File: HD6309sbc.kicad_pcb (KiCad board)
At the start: 2 copper layers, 99.8 x 99.8 mm, 29 parts, among them J1 Conn_01x02_Male, J2 Conn_02x30_Odd_Even, J3 Conn_01x02_Male, U1 HD63C09, U10 74HC375, U11 74HC02, U12 74HC21, U13 74HC21, U2 74HC163, U3 74HC04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

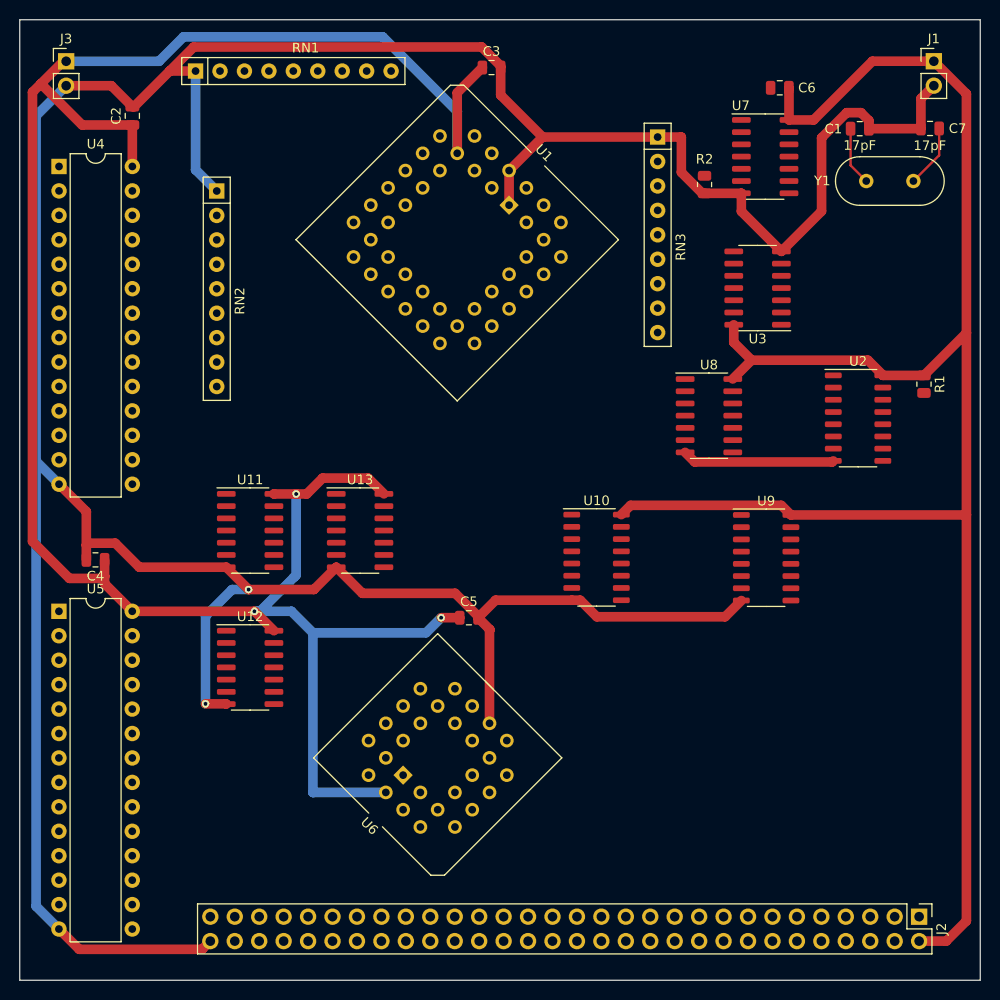
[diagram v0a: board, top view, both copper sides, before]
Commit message: add paged memory
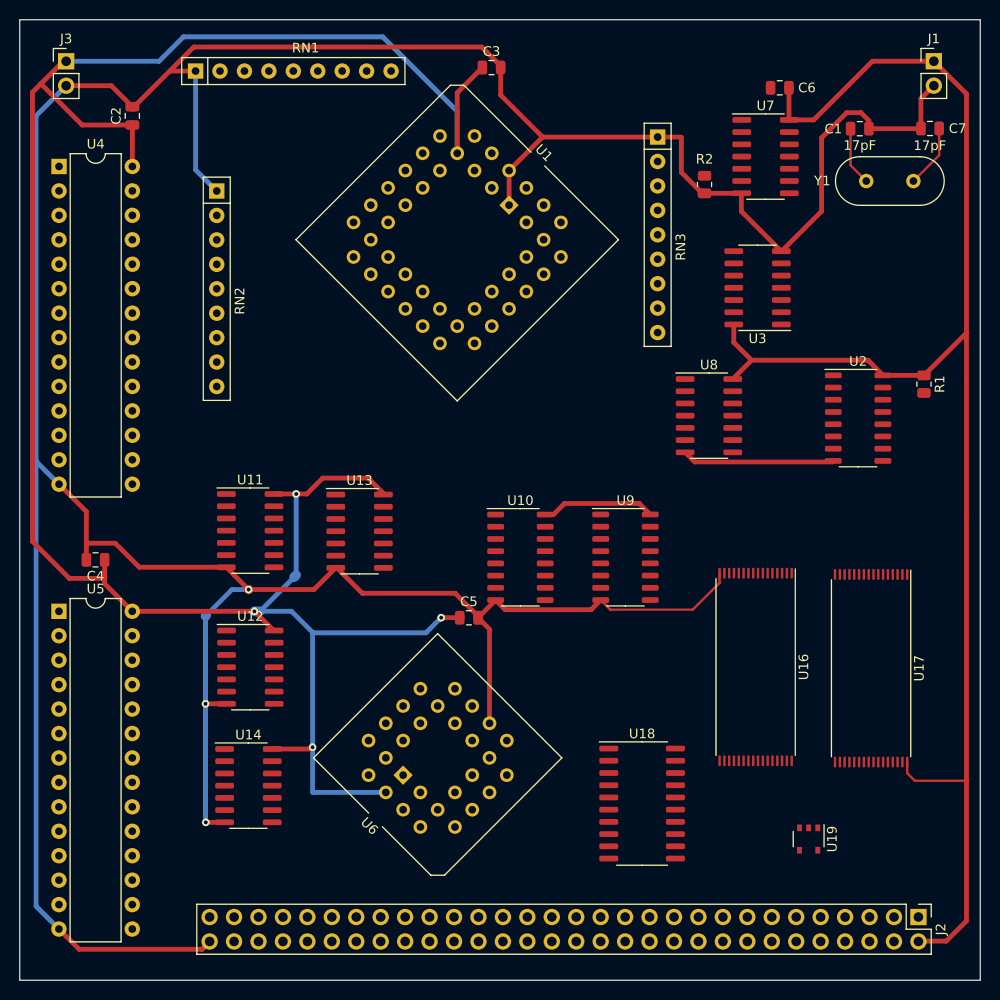
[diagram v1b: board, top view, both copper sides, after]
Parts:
- added U14: 74HC02, Package_SO:SO-14_3.9x8.65mm_P1.27mm, F.Cu at (49.2, 105.0)
- added U16: AS6C4008-55PCN, Package_SO:TSOP-I-32_18.4x8mm_P0.5mm, F.Cu at (101.9, 92.7)
- added U17: AS6C4008-55PCN, Package_SO:TSOP-I-32_18.4x8mm_P0.5mm, F.Cu at (113.9, 92.8)
- added U18: 74LS244, Package_SO:SO-20_5.3x12.6mm_P1.27mm, F.Cu at (90.1, 106.9)
- added U19: 74AHC1G86, Package_SO:TSOP-5_1.65x3.05mm_P0.95mm, F.Cu at (107.4, 110.5)
- U3: value 74HC04 -> 74HC02
- moved U9 14.6 mm to (88.3, 81.3)
- moved U10 7.91 mm to (77.4, 81.3)
- moved U13 0.09 mm to (60.7, 78.6)
- moved J2 0.08 mm to (118.8, 118.6)
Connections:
- U3 pad 1: Net-(C1-Pad1) -> E
- U3 pad 10: unconnected-(U3-Pad10) -> ~{E}
- U3 pad 11: unconnected-(U3-Pad11) -> Clock3
- U3 pad 12: unconnected-(U3-Pad12) -> Clock3
- U3 pad 13: unconnected-(U3-Pad13) -> ~{Q}
- U3 pad 2: Net-(U3-Pad2) -> Clock3
- U3 pad 3: Net-(U3-Pad2) -> Clock6
- U3 pad 5: Clock12 -> Net-(C1-Pad1)
- U3 pad 6: ~{Clock12} -> Net-(C1-Pad1)
- U3 pad 8: unconnected-(U3-Pad8) -> E
- U3 pad 9: unconnected-(U3-Pad9) -> E
- U7 pad 10: unconnected-(U7-Pad10) -> Net-(U7-Pad10)
- U7 pad 11: unconnected-(U7-Pad11) -> A15
- U7 pad 12: unconnected-(U7-Pad12) -> Net-(U7-Pad12)
- U7 pad 13: unconnected-(U7-Pad13) -> P5
- U8 pad 10: unconnected-(U8-Pad10) -> Net-(U7-Pad10)
- U8 pad 8: unconnected-(U8-Pad8) -> ~{BS}
- U8 pad 9: unconnected-(U8-Pad9) -> A14
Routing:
- net GND: track 386.4 -> 400.0 mm, vias 2 -> 3
- net +5V: track 418.0 -> 404.8 mm, vias 3 -> 4

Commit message: add power routing
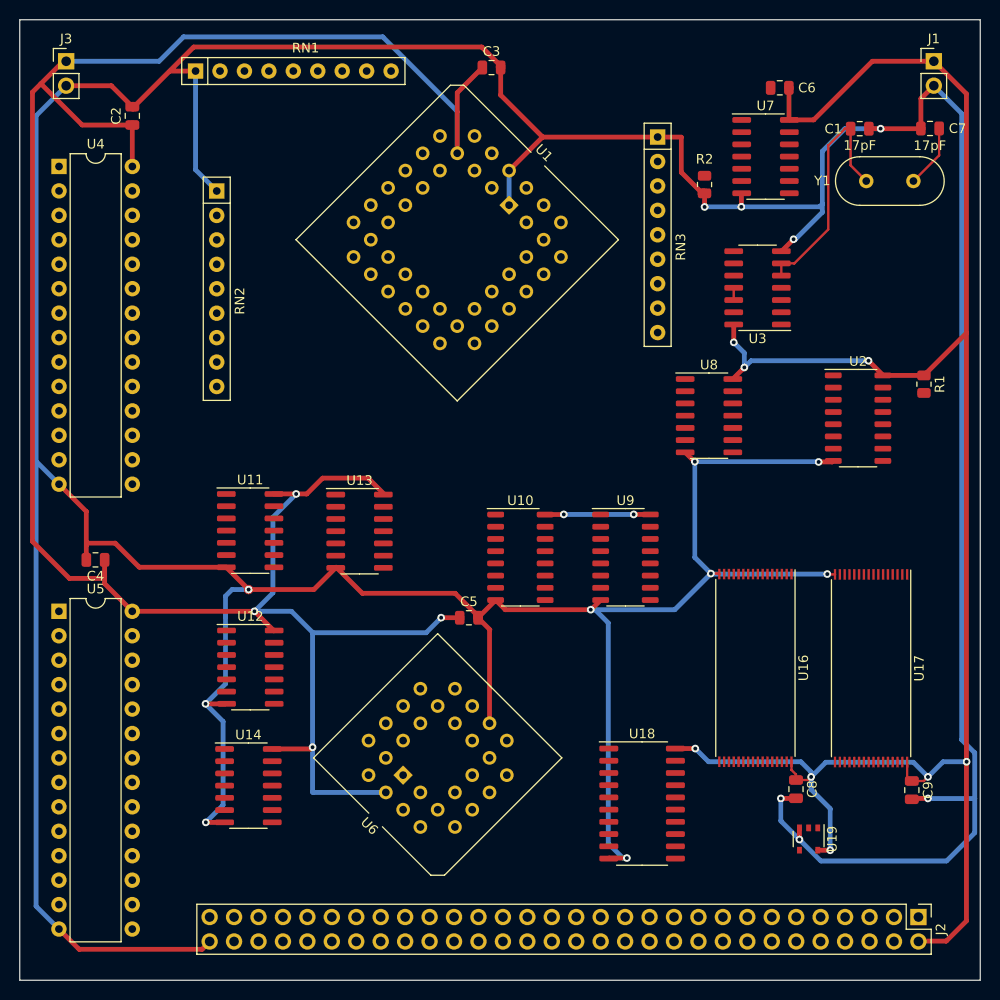
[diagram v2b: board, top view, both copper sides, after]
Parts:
- added C8: 1uF, Capacitor_SMD:C_0805_2012Metric, F.Cu at (106.1, 105.4)
- added C9: 1uF, Capacitor_SMD:C_0805_2012Metric, F.Cu at (118.1, 105.5)
- C3: value C -> 1uF
- moved U16 0.10 mm to (101.9, 92.8)
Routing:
- net GND: track 400.0 -> 572.9 mm, vias 3 -> 16
- net +5V: track 404.8 -> 447.9 mm, vias 4 -> 14
- net Net-(C1-Pad1): track 6.11 -> 25.5 mm
- net Clock3: track 0.00 -> 1.27 mm

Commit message: move rom for clearance
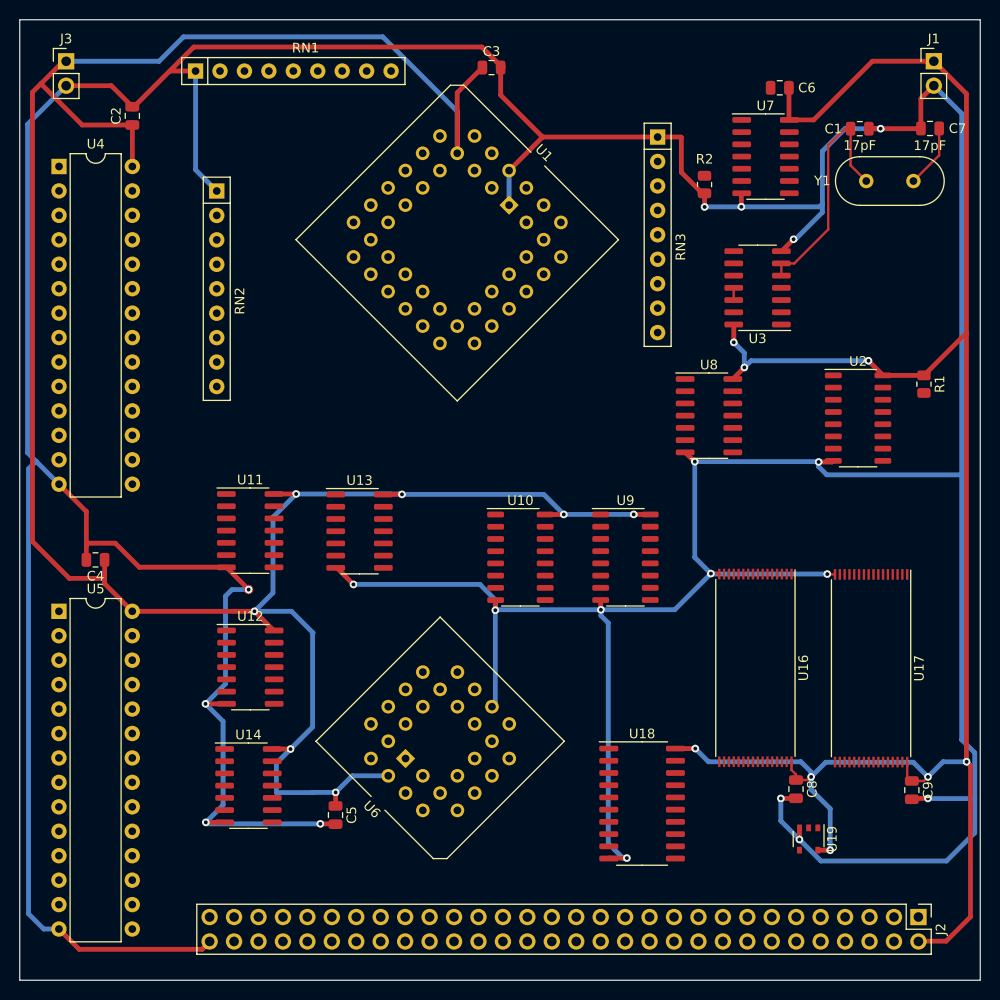
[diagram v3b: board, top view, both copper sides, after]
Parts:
- moved C5 24.7 mm to (58.2, 108.1), turned to -90 degrees
- moved U6 1.75 mm to (65.5, 102.2)
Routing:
- net GND: track 572.9 -> 592.2 mm, vias 16 -> 19
- net +5V: track 447.9 -> 457.8 mm, vias 14 -> 15

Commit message: rearrange components for routing
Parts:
- moved RN1 105.6 mm to (108.7, 113.9), turned to 180 degrees
- moved RN3 87.8 mm to (109.6, 123.5), turned to 180 degrees
- moved RN2 82.7 mm to (65.5, 123.5), turned to 0 degrees
- moved C5 77.9 mm to (47.5, 30.9), turned to 180 degrees
- moved U6 65.1 mm to (53.4, 38.2), turned to 45 degrees
- moved U1 46.9 mm to (73.3, 91.5)
- moved C3 45.9 mm to (69.8, 76.0)
- moved U18 23.6 mm to (86.2, 83.6), turned to -90 degrees
- moved U9 16.0 mm to (82.3, 66.4)
- moved U10 16.0 mm to (71.4, 66.5)
- moved U13 12.5 mm to (56.0, 67.0)
- moved U11 11.8 mm to (46.7, 67.0)
- moved U12 11.8 mm to (46.7, 81.2)
- moved U14 11.8 mm to (46.5, 93.5)
- moved C9 3.71 mm to (118.5, 101.8)
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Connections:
- J2 pad 35: Q3 -> unconnected-(J2-Pad35)
- J2 pad 37: Q4 -> unconnected-(J2-Pad37)
- J2 pad 39: Q5 -> unconnected-(J2-Pad39)
- J2 pad 41: Q6 -> unconnected-(J2-Pad41)
- J2 pad 43: Q7 -> unconnected-(J2-Pad43)
- RN2 pad 2: A13 -> A15
- RN2 pad 3: A8 -> A14
- RN2 pad 4: A9 -> A13
- RN2 pad 5: A11 -> A12
- RN2 pad 6: A10 -> A11
- RN2 pad 7: A15 -> A10
- RN2 pad 8: A1 -> A9
- RN2 pad 9: A0 -> A8
- RN3 pad 2: A2 -> A0
- RN3 pad 3: A3 -> A1
- RN3 pad 4: A12 -> A2
- RN3 pad 5: A14 -> A3
- U10 pad 11: Q6 -> P3
- U10 pad 13: Q7 -> P4
- U10 pad 3: Q4 -> P1
- U10 pad 5: Q5 -> P2
- U9 pad 13: Q3 -> P0
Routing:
- net +5V: track 457.8 -> 522.5 mm, vias 15 -> 18
- net GND: track 592.2 -> 643.8 mm, vias 19 -> 22

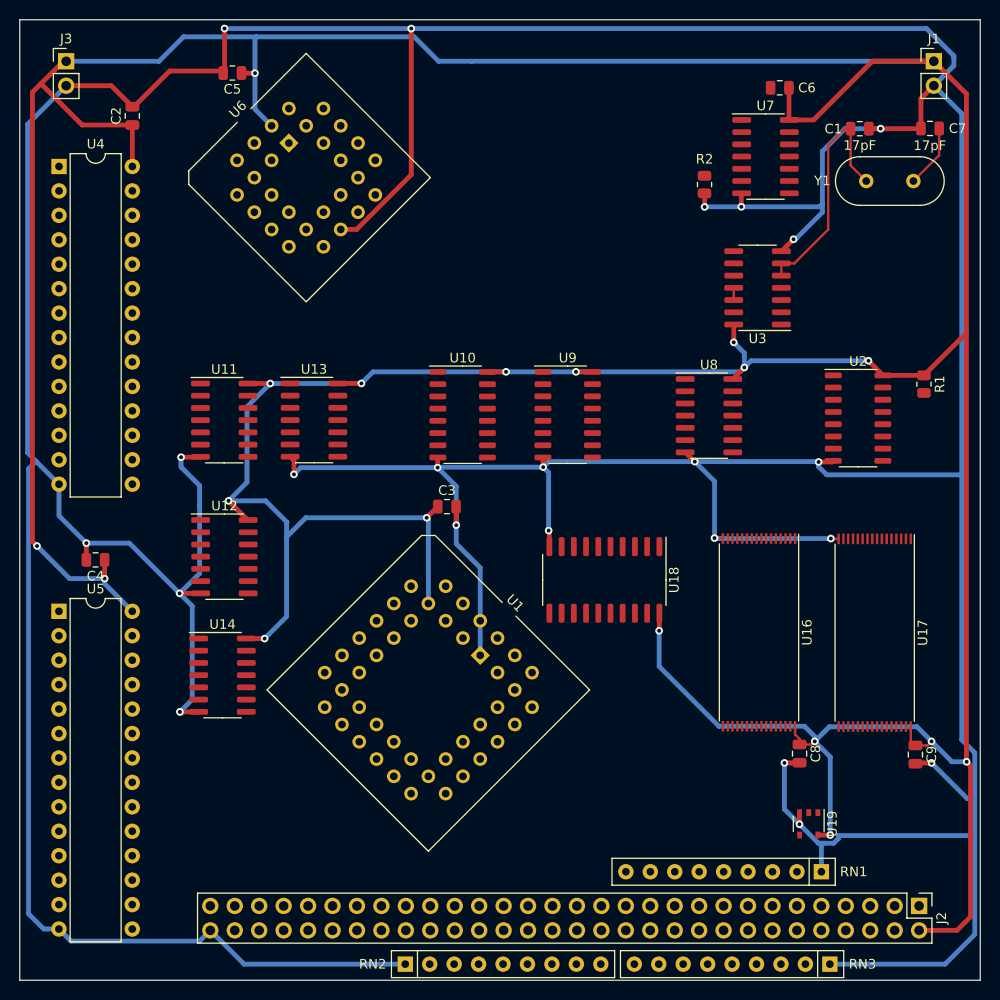
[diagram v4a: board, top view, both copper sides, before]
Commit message: reduce component count
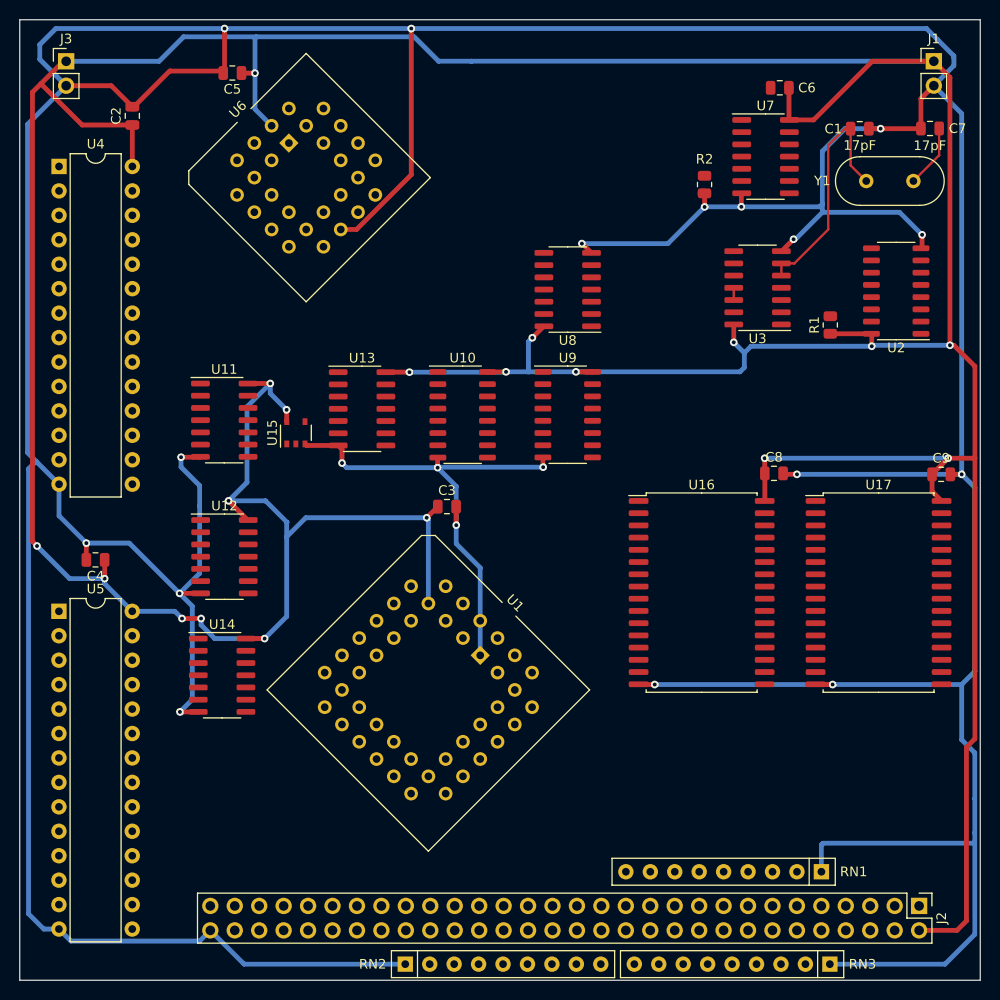
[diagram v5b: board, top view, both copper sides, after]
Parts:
- removed U18: 74LS244, Package_SO:SO-20_5.3x12.6mm_P1.27mm
- removed U19: 74AHC1G86, Package_SO:TSOP-5_1.65x3.05mm_P0.95mm
- added U15: 74AHC1G08, Package_SO:TSOP-5_1.65x3.05mm_P0.95mm, F.Cu at (54.1, 68.3)
- U16, U17: footprint Package_SO:TSOP-I-32_18.4x8mm_P0.5mm -> Package_SO:SSOP-32_11.305x20.495mm_P1.27mm
- moved C9 29.2 mm to (121.2, 72.6), turned to 0 degrees
- moved C8 29.2 mm to (103.8, 72.5), turned to 0 degrees
- moved U8 19.7 mm to (82.3, 53.4), turned to 180 degrees
- moved U2 13.8 mm to (116.5, 53.6), turned to 180 degrees
- moved R1 11.5 mm to (109.6, 57.1), turned to 90 degrees
- moved U16 7.25 mm to (96.3, 84.9), turned to 0 degrees
- moved U13 5.13 mm to (61.0, 65.8)
- moved U17 4.19 mm to (114.7, 84.9), turned to 0 degrees
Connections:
- U11 pad 11: A6 -> unconnected-(U11-Pad11)
- U11 pad 12: A7 -> unconnected-(U11-Pad12)
- U11 pad 13: Net-(U11-Pad13) -> unconnected-(U11-Pad13)
- U11 pad 5: A2 -> A3
- U11 pad 6: A3 -> A4
- U11 pad 8: A4 -> A6
- U11 pad 9: A5 -> A7
- U13 pad 5: Net-(U11-Pad13) -> Net-(U13-Pad5)
- U14 pad 1: ~{OEa} -> (no net)
- U14 pad 2: Net-(U14-Pad2) -> (no net)
- U14 pad 3: ~{OE} -> (no net)
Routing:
- net +5V: track 522.5 -> 502.2 mm, vias 18 -> 19
- net GND: track 643.8 -> 652.3 mm, vias 22 -> 20

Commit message: move paged memory to external board
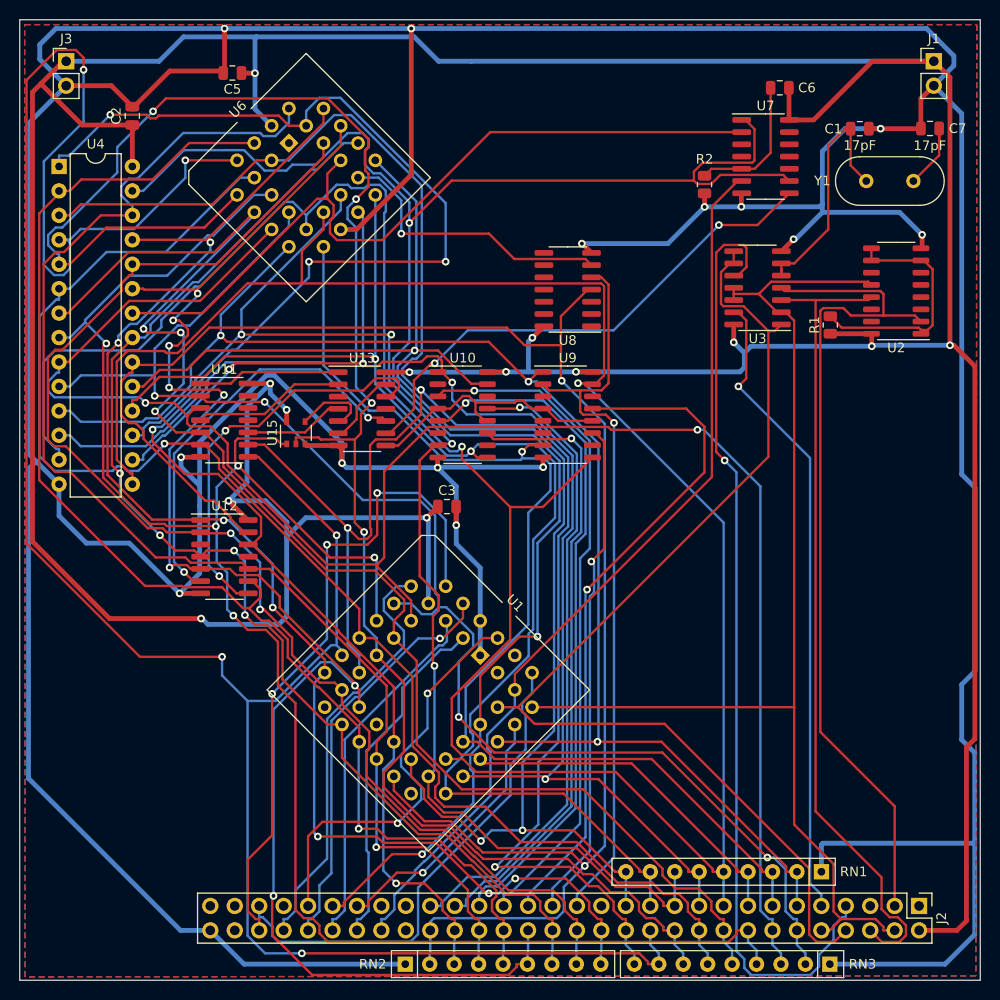
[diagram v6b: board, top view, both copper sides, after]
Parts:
- removed C4, C8, C9: 1uF, Capacitor_SMD:C_0805_2012Metric
- removed U14: 74HC02, Package_SO:SO-14_3.9x8.65mm_P1.27mm
- removed U16, U17: AS6C4008-55PCN, Package_SO:SSOP-32_11.305x20.495mm_P1.27mm
- removed U5: UM61256FK, Package_DIP:DIP-28_W7.62mm
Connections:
- J2 pad 35: unconnected-(J2-Pad35) -> Q3
- J2 pad 37: unconnected-(J2-Pad37) -> Q4
- J2 pad 39: unconnected-(J2-Pad39) -> Q5
- J2 pad 41: unconnected-(J2-Pad41) -> Q6
- J2 pad 43: unconnected-(J2-Pad43) -> Q7
- J2 pad 45: unconnected-(J2-Pad45) -> Q8
- U10 pad 11: P3 -> Q5
- U10 pad 13: P4 -> Q6
- U10 pad 3: P1 -> Q3
- U10 pad 5: P2 -> Q4
- U7 pad 10: Net-(U7-Pad10) -> (no net)
- U7 pad 11: A15 -> (no net)
- U7 pad 12: Net-(U14-Pad6) -> (no net)
- U7 pad 13: P5 -> (no net)
- U8 pad 1: A15 -> unconnected-(U8-Pad1)
- U8 pad 10: Net-(U7-Pad10) -> (no net)
- U8 pad 2: ~{ROM}/RAM -> unconnected-(U8-Pad2)
- U8 pad 3: Net-(U5-Pad20) -> unconnected-(U8-Pad3)
- U8 pad 8: ~{BS} -> (no net)
- U8 pad 9: A14 -> (no net)
- U9 pad 11: Q2 -> Q1
- U9 pad 13: P0 -> Q2
- U9 pad 2: ~{ROM}/RAM -> ROM/~{RAM}
- U9 pad 3: ROM/~{RAM} -> ~{ROM}/RAM
- U9 pad 5: Q1 -> Q0
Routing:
- net A6: track 0.00 -> 248.7 mm, vias 0 -> 5
- net A7: track 0.00 -> 204.9 mm, vias 0 -> 3
- net A2: track 0.00 -> 197.7 mm, vias 0 -> 5
- net R/~{W}: track 0.00 -> 192.6 mm, vias 0 -> 3
- net A5: track 0.00 -> 188.8 mm, vias 0 -> 4
- net A1: track 0.00 -> 188.3 mm, vias 0 -> 2
- net A15: track 0.00 -> 185.0 mm, vias 0 -> 2
- net D3: track 0.00 -> 183.8 mm, vias 0 -> 1
- net D2: track 0.00 -> 175.5 mm, vias 0 -> 1
- net A14: track 0.00 -> 170.2 mm, vias 0 -> 5
- net A11: track 0.00 -> 165.1 mm, vias 0 -> 8
- net D7: track 0.00 -> 159.5 mm, vias 0 -> 3
- net A3: track 0.00 -> 152.1 mm, vias 0 -> 3
- net D0: track 0.00 -> 151.8 mm, vias 0 -> 3
- net A0: track 0.00 -> 150.8 mm, vias 0 -> 4
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- added copper zone on B.Cu, net (none)
- added copper zone on F.Cu, net (none)
